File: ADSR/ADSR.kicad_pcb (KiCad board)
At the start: 2 copper layers, 25 x 200 mm, 52 parts, among them J1 EuroPower, J2 GATE, J3 Hard Envelope, J4 Envelope, Q1 BC557, Q2 BC547, Q3 BC547, Q4 BC547, U1 LM741, U2 LM741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

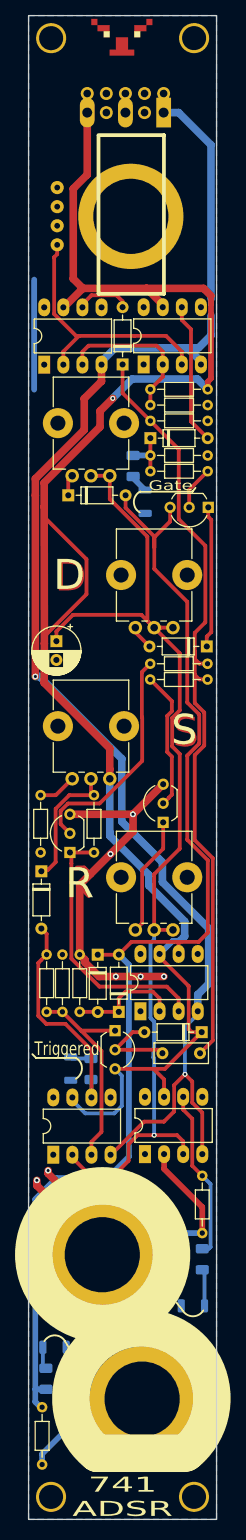
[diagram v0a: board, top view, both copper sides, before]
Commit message: More clearance
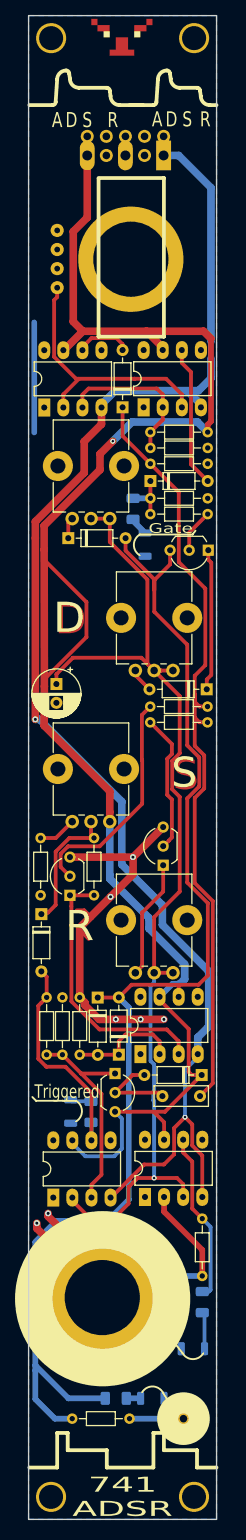
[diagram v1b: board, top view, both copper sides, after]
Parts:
- J3: footprint telec:Jack_Hole_Square -> Connector_PinSocket_2.54mm:PinSocket_1x01_P2.54mm_Vertical
- moved D11 14.7 mm to (28.4, 195.9)
- moved R15 9.66 mm to (23.6, 195.9), turned to 0 degrees
- moved J3 6.08 mm to (32.6, 198.6)
- moved D1 5.70 mm to (35.0, 152.9)
- moved D12 5.70 mm to (33.9, 189.3)
- moved R10 5.70 mm to (18.8, 142.6)
- moved R14 5.70 mm to (20.3, 157.8)
- moved R4 5.70 mm to (14.4, 142.6)
- moved RV4 5.70 mm to (31.2, 139.3)
- moved U4 5.70 mm to (26.9, 150.1)
- moved U5 5.70 mm to (27.5, 169.1)
- moved C2 5.70 mm to (15.7, 100.9)
- moved D2 5.70 mm to (28.2, 73.9)
- moved D4 5.70 mm to (13.7, 131.5)
- moved D7 5.70 mm to (17.3, 81.5)
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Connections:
- R18 pad 2: Net-(J3-PadT) -> Net-(J3-Pad1)
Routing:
- net /Hard: track 159.5 -> 167.8 mm
- net Net-(J3-Pad1): track 0.00 -> 7.18 mm
- net Net-(J3-PadT): track 6.38 -> 0.00 mm
- net Net-(D11-Pad2): track 2.97 -> 1.90 mm
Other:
- board text added: "A"
- board text added: "GATE"
